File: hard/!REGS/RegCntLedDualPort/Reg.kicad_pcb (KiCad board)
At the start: 2 copper layers, 71.1 x 42.5 mm, 41 parts, among them J1 Conn_01x08_Male, J10 Conn_01x01_Male, J11 Conn_01x08_Male, J2 Conn_01x08_Male, J3 Conn_01x02_Male, J4 Conn_01x03_Male, J5 Conn_01x02_Male, J6 Conn_01x02_Male, J7 Conn_01x01_Male, J8 Conn_01x01_Male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

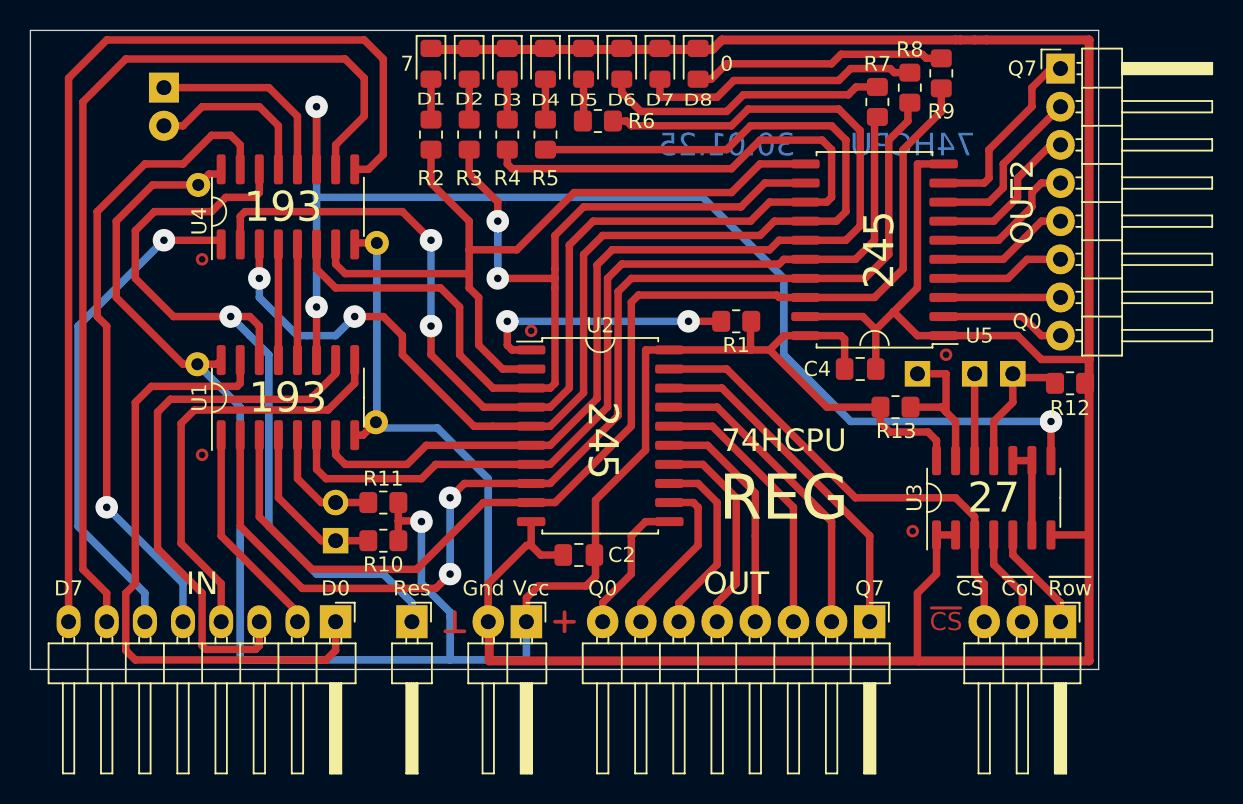
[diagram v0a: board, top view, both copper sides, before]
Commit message: KiCAD 5 -> 9
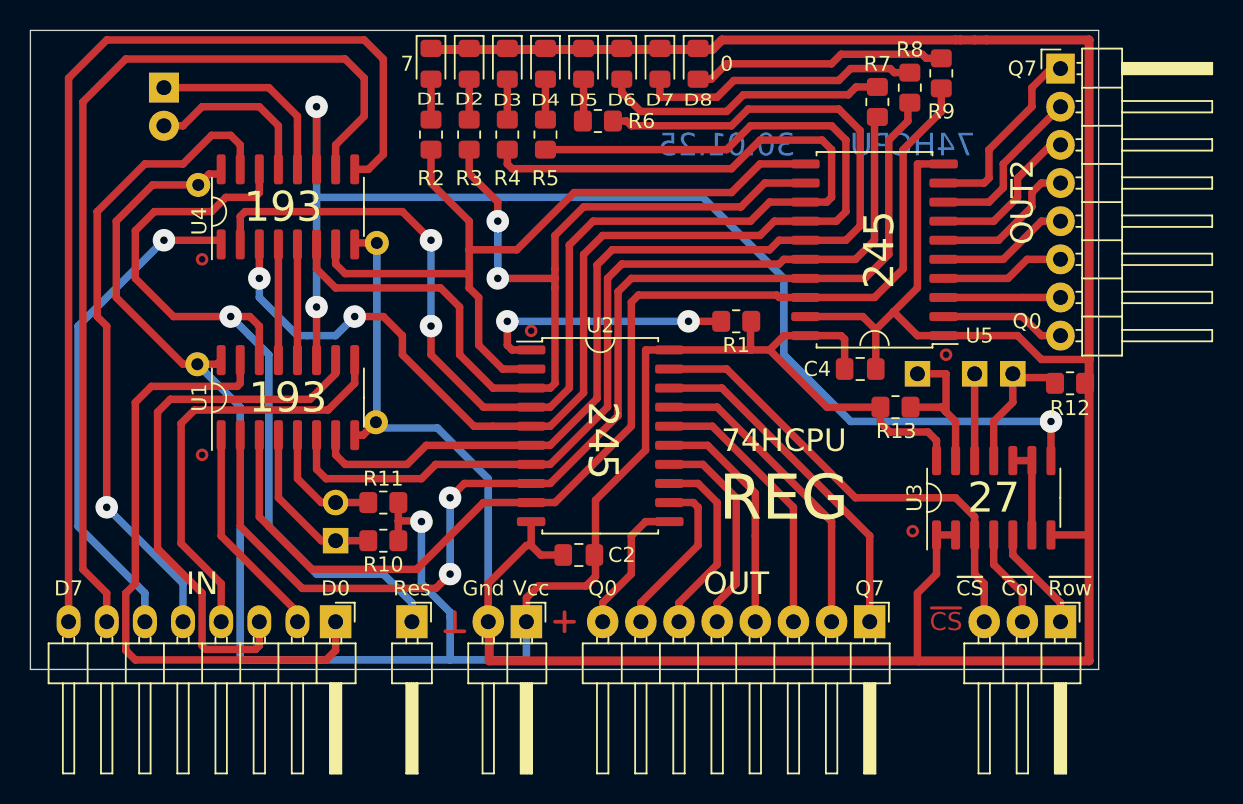
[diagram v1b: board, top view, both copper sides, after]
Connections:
- net /~CS renamed /~{CS}
- net /~Col renamed /~{Col}
- net /~LOAD renamed /~{LOAD}
- net /~MLOAD renamed /~{MLOAD}
- net /~Row renamed /~{Row}
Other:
- net class Default removed
- board text added: "Connect this to use ~{MLOAD}"
- board text added: "~{CS}"
- board text added: "~{Col}"
- board text added: "~{MLOAD}"
- board text added: "~{Row}"
- board text removed: "Connect this to use ~MLOAD"
- board text removed: "~CS"
- board text removed: "~Col"
- board text removed: "~MLOAD"
- board text removed: "~Row"
